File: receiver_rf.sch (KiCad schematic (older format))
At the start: 27 parts, among them J6 Conn_Coaxial, J7 Conn_Coaxial, J8 Conn_Coaxial, U13 PMA-63GLN+, U14 QPC6324, U15 PMA-63GLN+, U16 QPC6324, U17 HMC218BMS8GE

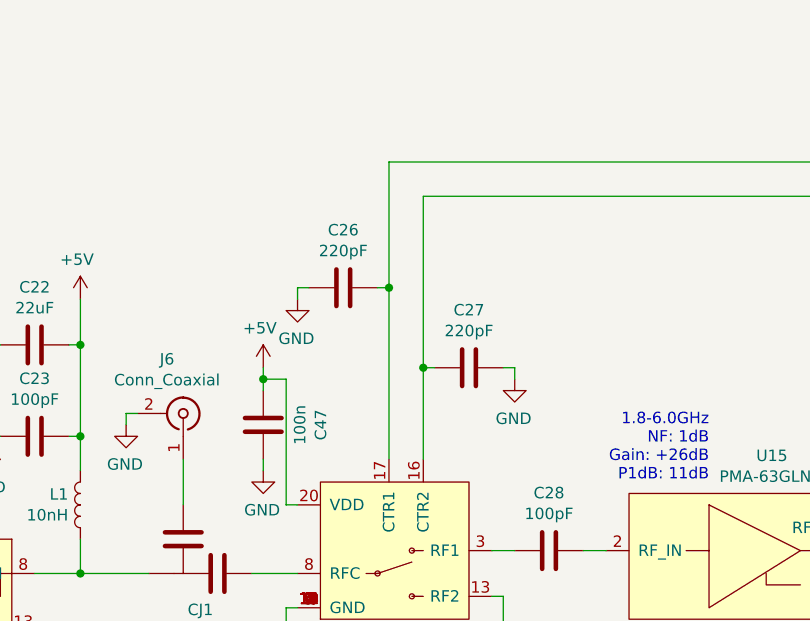
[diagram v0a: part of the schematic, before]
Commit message: IF and power layout mostly finished
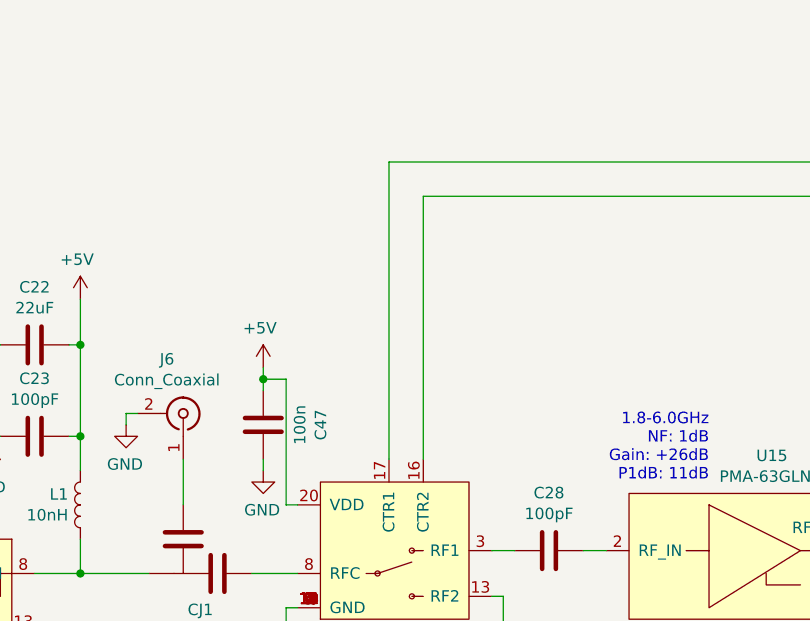
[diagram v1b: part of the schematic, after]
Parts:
- removed C26, C27: 220pF, Capacitor_SMD:C_0603_1608Metric_Pad1.08x0.95mm_HandSolder, symbol Device:C
- J6, J7, J8: footprint Connector_Coaxial:SMA_Amphenol_901-144_Vertical -> Connector_Coaxial:SMA_Amphenol_132134-11_Vertical
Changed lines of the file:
@@
 F 0 "J6" V 3787 3529 50  0000 C CNN
 F 1 "Conn_Coaxial" V 3696 3529 50  0000 C CNN
-F 2 "Connector_Coaxial:SMA_Amphenol_901-144_Vertical" H 3550 3600 50  0001 C CNN
+F 2 "Connector_Coaxial:SMA_Amphenol_132134-11_Vertical" H 3550 3600 50  0001 C CNN
 F 3 " ~" H 3550 3600 50  0001 C CNN
 	1    3550 3600
@@
 Wire Wire Line
 	7750 3700 7750 3350
-Wire Wire Line
-	4600 2650 4600 3400
-Wire Wire Line
-	4450 3800 4450 3050
 $Comp
 L power:+5V #PWR047
@@
 Wire Wire Line
 	8300 2900 8300 2950
-$Comp
-L Device:C C27
-U 1 1 60493731
-P 4800 3400
-F 0 "C27" V 4548 3400 50  0000 C CNN
-F 1 "220pF" V 4639 3400 50  0000 C CNN
-F 2 "Capacitor_SMD:C_0603_1608Metric_Pad1.08x0.95mm_HandSolder" H 4838 3250 50  0001 C CNN
-F 3 "~" H 4800 3400 50  0001 C CNN
-	1    4800 3400
-	0    -1   1    0
-$EndComp
-$Comp
-L power:GND #PWR040
-U 1 1 60493737
-P 4050 3100
-F 0 "#PWR040" H 4050 2850 50  0001 C CNN
-F 1 "GND" H 4055 2927 50  0000 C CNN
-F 2 "" H 4050 3100 50  0001 C CNN
-F 3 "" H 4050 3100 50  0001 C CNN
-	1    4050 3100
-	-1   0    0    -1
-$EndComp
-Wire Wire Line
-	4050 3100 4050 3050
-Wire Wire Line
-	4050 3050 4100 3050
-Wire Wire Line
-	4400 3050 4450 3050
-$Comp
-L Device:C C26
-U 1 1 60495DDF
-P 4250 3050
-F 0 "C26" V 3998 3050 50  0000 C CNN
-F 1 "220pF" V 4089 3050 50  0000 C CNN
-F 2 "Capacitor_SMD:C_0603_1608Metric_Pad1.08x0.95mm_HandSolder" H 4288 2900 50  0001 C CNN
-F 3 "~" H 4250 3050 50  0001 C CNN
-	1    4250 3050
-	0    -1   1    0
-$EndComp
-Wire Wire Line
-	4600 3400 4650 3400
-$Comp
-L power:GND #PWR041
-U 1 1 60495DE6
-P 5000 3450
-F 0 "#PWR041" H 5000 3200 50  0001 C CNN
-F 1 "GND" H 5005 3277 50  0000 C CNN
-F 2 "" H 5000 3450 50  0001 C CNN
-F 3 "" H 5000 3450 50  0001 C CNN
-	1    5000 3450
-	-1   0    0    -1
-$EndComp
-Wire Wire Line
-	4950 3400 5000 3400
-Wire Wire Line
-	5000 3400 5000 3450
-Connection ~ 4600 3400
-Wire Wire Line
-	4600 3400 4600 3800
-Connection ~ 4450 3050
-Wire Wire Line
-	4450 3050 4450 2500
 Text HLabel 7750 2200 1    50   Input ~ 0
 SW_CTR1
@@
 F 0 "J7" V 9087 3429 50  0000 C CNN
 F 1 "Conn_Coaxial" V 8996 3429 50  0000 C CNN
-F 2 "Connector_Coaxial:SMA_Amphenol_901-144_Vertical" H 8850 3500 50  0001 C CNN
+F 2 "Connector_Coaxial:SMA_Amphenol_132134-11_Vertical" H 8850 3500 50  0001 C CNN
 F 3 " ~" H 8850 3500 50  0001 C CNN
 	1    8850 3500
@@
 F 0 "J8" V 10037 2929 50  0000 C CNN
 F 1 "Conn_Coaxial" V 9946 2929 50  0000 C CNN
-F 2 "Connector_Coaxial:SMA_Amphenol_901-144_Vertical" H 9800 3000 50  0001 C CNN
+F 2 "Connector_Coaxial:SMA_Amphenol_132134-11_Vertical" H 9800 3000 50  0001 C CNN
 F 3 " ~" H 9800 3000 50  0001 C CNN
 	1    9800 3000
@@
 Wire Wire Line
 	9100 3300 9100 3850
+Wire Wire Line
+	4450 2500 4450 3800
+Wire Wire Line
+	4600 2650 4600 3800
 $EndSCHEMATC

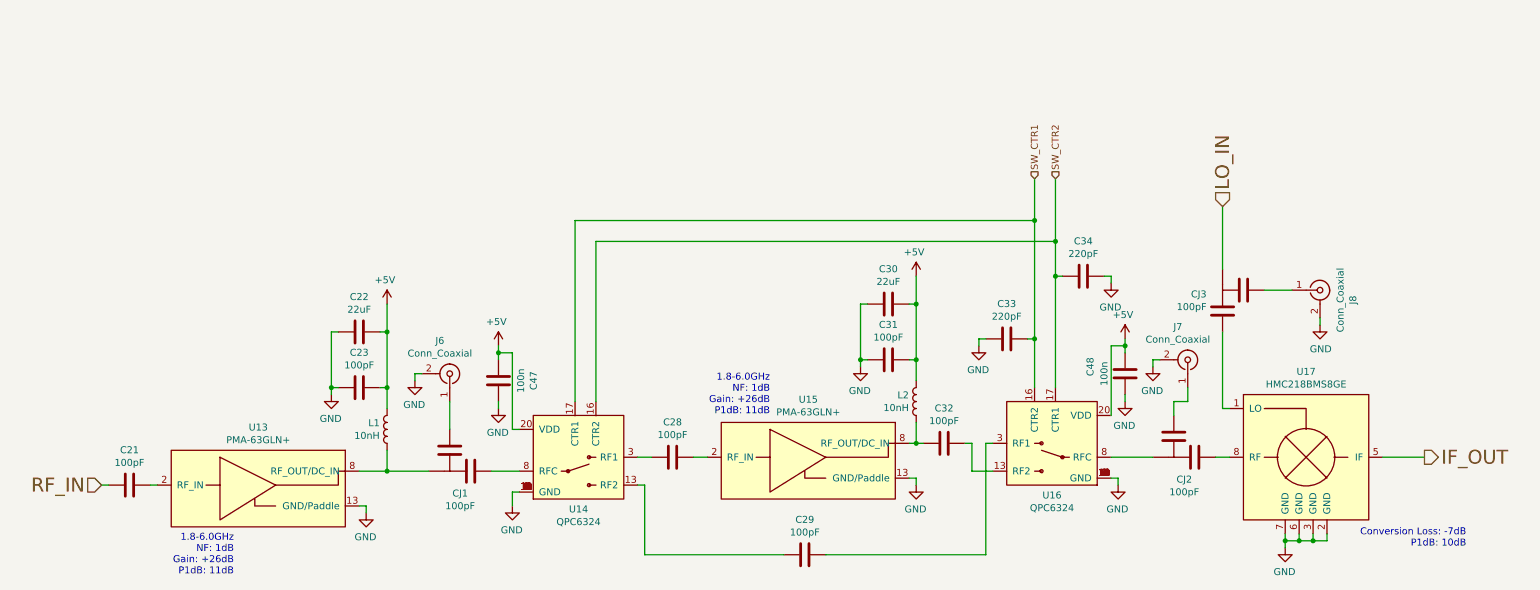
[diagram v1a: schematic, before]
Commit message: Added RX shield
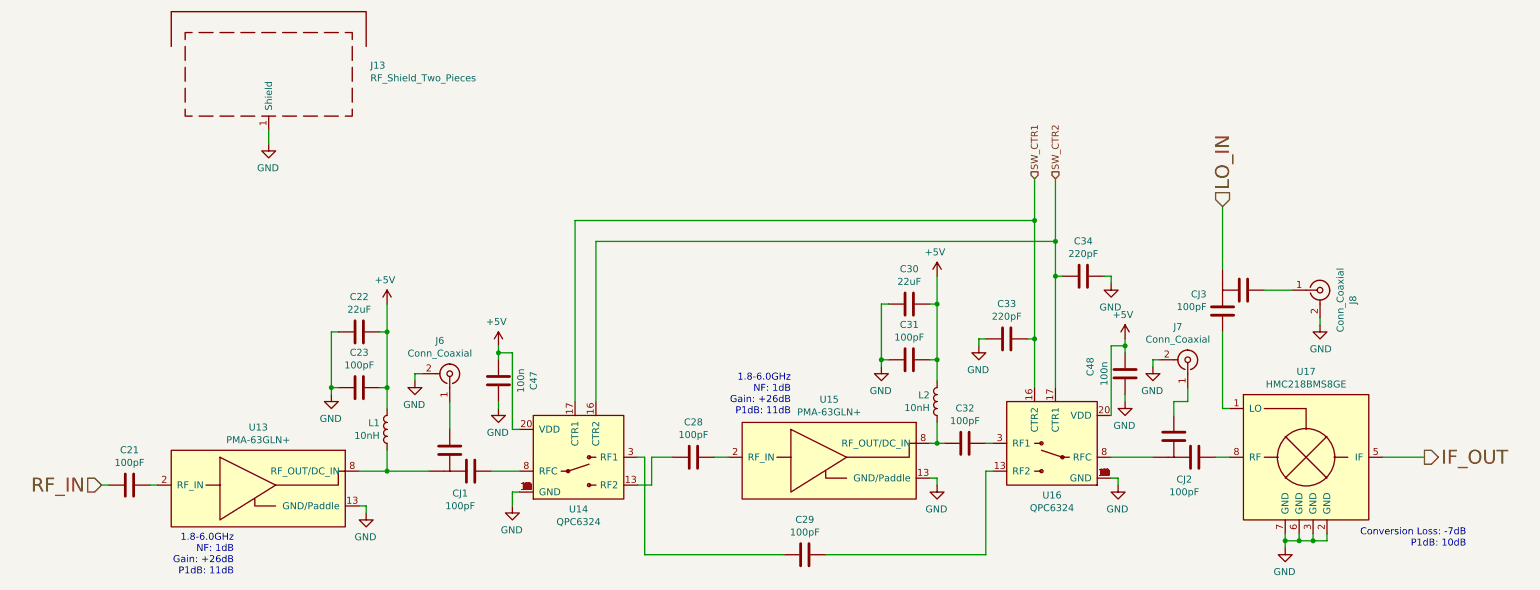
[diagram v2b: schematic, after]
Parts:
- added J13: RF_Shield_Two_Pieces, RF_Shielding:Laird_Technologies_BMI-S-209-F_29.36x18.50mm, symbol Device:RF_Shield_Two_Pieces
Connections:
- net GND: now also J13.1 (Shield)
- net at C28.1: now also U14.13 (RF2); no longer U14.3 (RF1)
- net at C32.2: now also U16.3 (RF1); no longer U16.13 (RF2)
- net at C29.1: now also U14.3 (RF1); no longer U14.13 (RF2)
- net at C29.2: now also U16.13 (RF2); no longer U16.3 (RF1)
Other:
- moved on the sheet: C28, C30, C31, C32, L2, U15
